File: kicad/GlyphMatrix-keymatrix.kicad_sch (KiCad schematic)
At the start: 153 parts

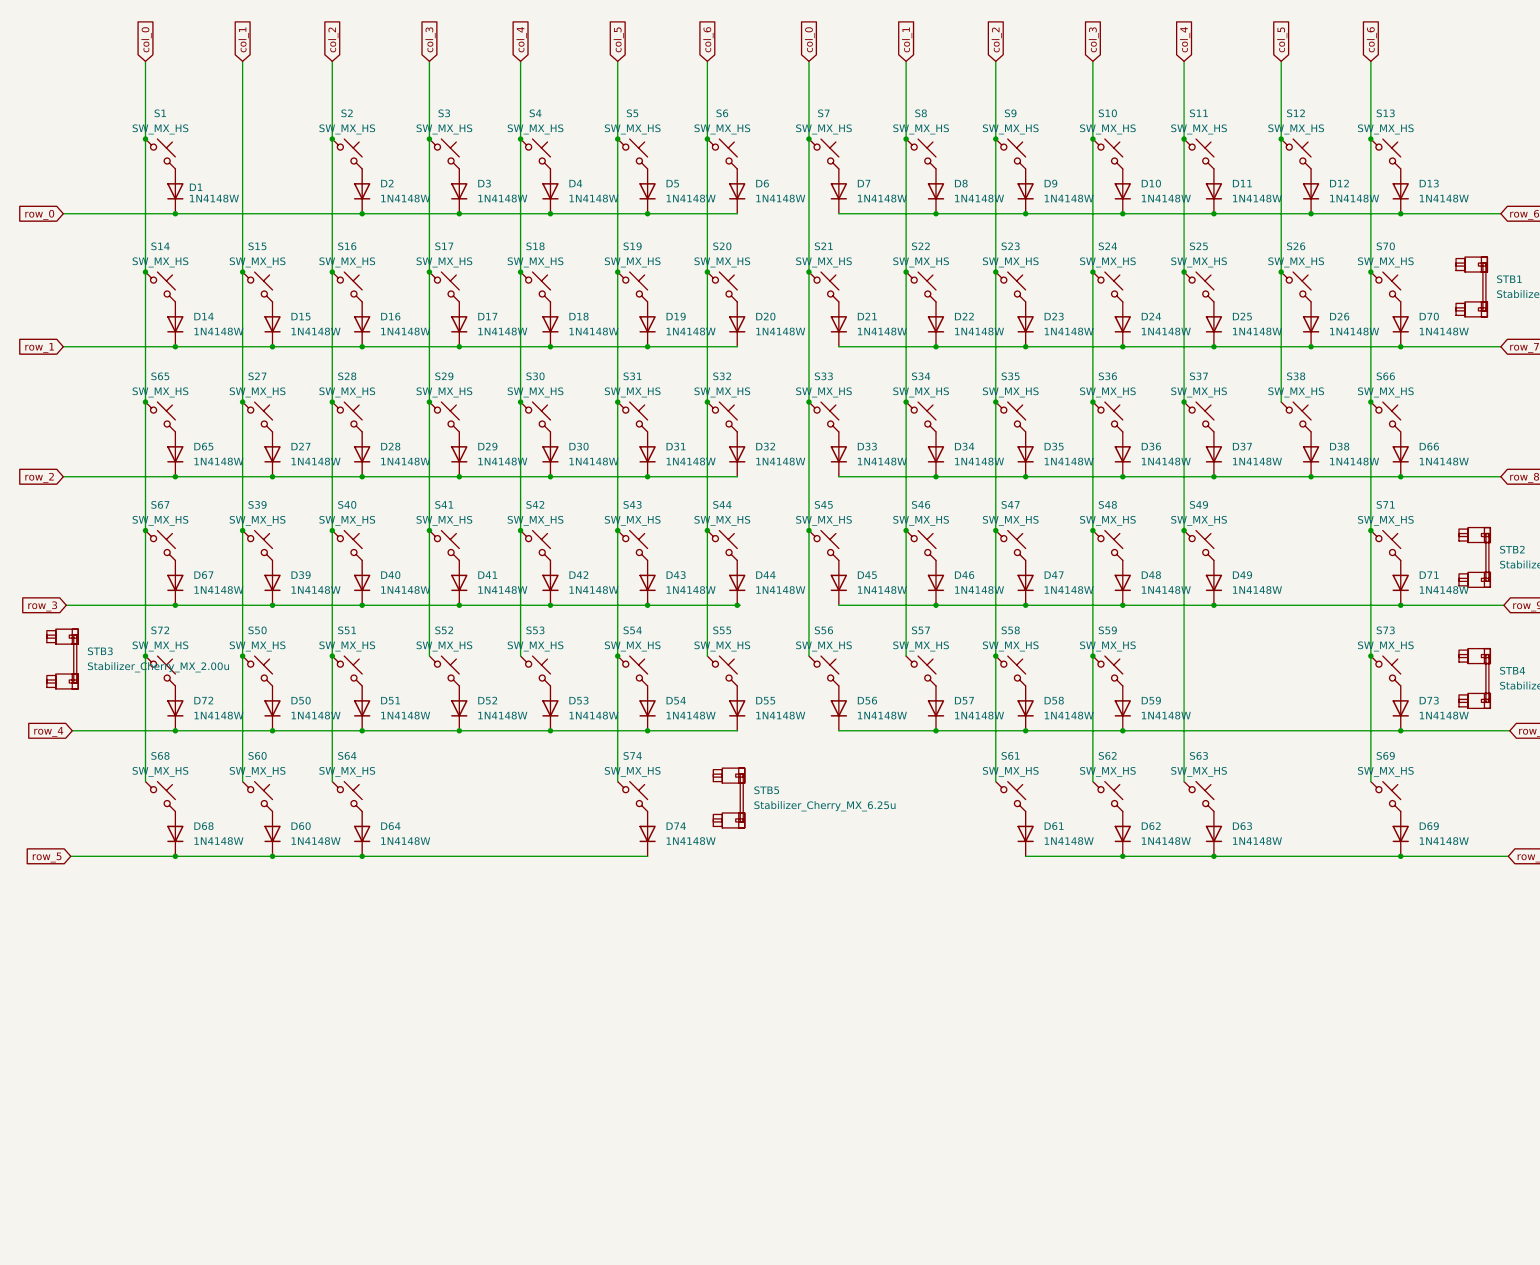
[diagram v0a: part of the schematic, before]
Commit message: added MCU
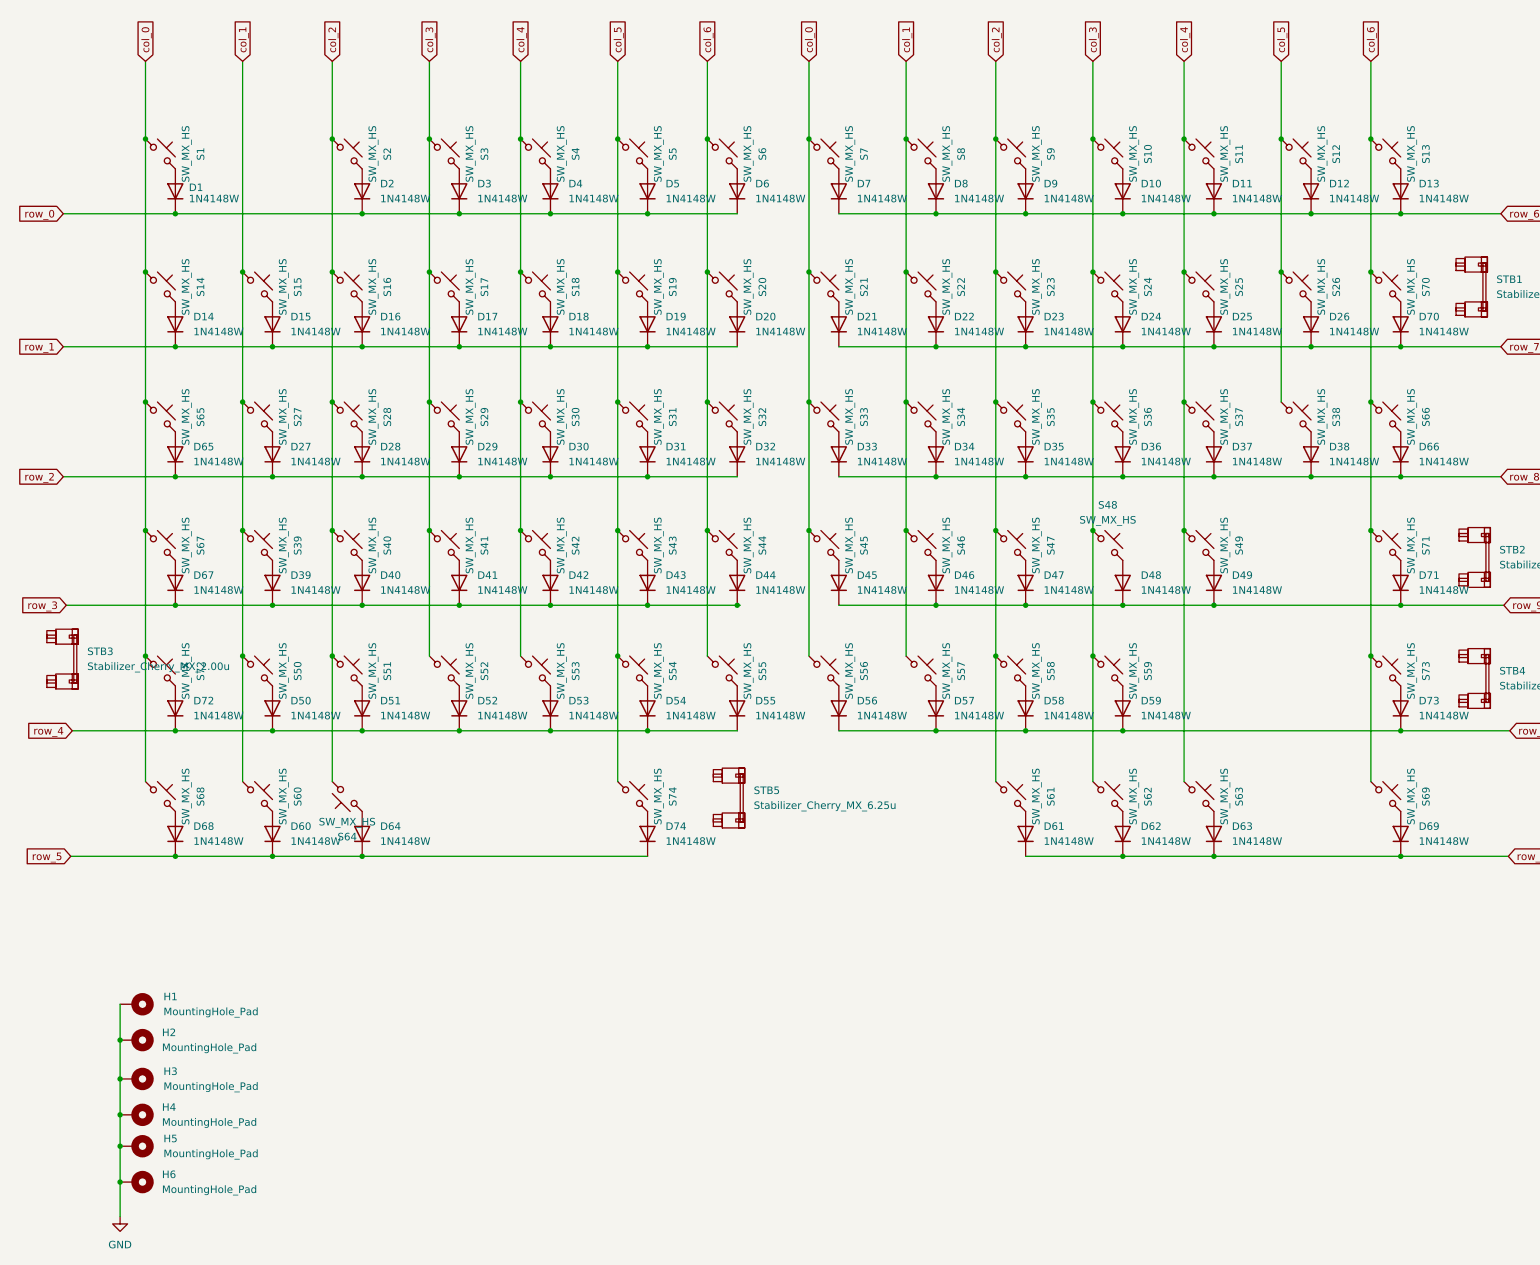
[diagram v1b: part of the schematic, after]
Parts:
- added H1, H2, H3, H4, H5, H6: MountingHole_Pad, TB2086_MISC:MountingHole_3.2mm_Pad, symbol TB2086_MISC:MountingHole_Pad
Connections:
- net col_0: now also S1.2, S14.2, S21.2, S33.2, S45.2, S56.2, S65.2, S67.2, S68.2, S7.2, S72.2; no longer S1.1, S14.1, S21.1, S33.1, S45.1, S56.1, S65.1, S67.1, S68.1, S7.1, S72.1
- net col_1: now also S15.2, S22.2, S27.2, S34.2, S39.2, S46.2, S50.2, S57.2, S60.2, S8.2; no longer S15.1, S22.1, S27.1, S34.1, S39.1, S46.1, S50.1, S57.1, S60.1, S8.1
- net col_2: now also S16.2, S2.2, S23.2, S28.2, S35.2, S40.2, S47.2, S51.2, S58.2, S61.2, S64.2, S9.2; no longer S16.1, S2.1, S23.1, S28.1, S35.1, S40.1, S47.1, S51.1, S58.1, S61.1, S64.1, S9.1
- net col_3: now also S10.2, S17.2, S24.2, S29.2, S3.2, S36.2, S41.2, S52.2, S59.2, S62.2; no longer S10.1, S17.1, S24.1, S29.1, S3.1, S36.1, S41.1, S52.1, S59.1, S62.1
- net col_4: now also S11.2, S18.2, S25.2, S30.2, S37.2, S4.2, S42.2, S49.2, S53.2, S63.2; no longer S11.1, S18.1, S25.1, S30.1, S37.1, S4.1, S42.1, S49.1, S53.1, S63.1
- net col_5: now also S12.2, S19.2, S26.2, S31.2, S38.2, S43.2, S5.2, S54.2, S74.2; no longer S12.1, S19.1, S26.1, S31.1, S38.1, S43.1, S5.1, S54.1, S74.1
- net col_6: now also S13.2, S20.2, S32.2, S44.2, S55.2, S6.2, S66.2, S69.2, S70.2, S71.2, S73.2; no longer S13.1, S20.1, S32.1, S44.1, S55.1, S6.1, S66.1, S69.1, S70.1, S71.1, S73.1
- net at D23.2 (A): now also S23.1; no longer S23.2
- net at D21.2 (A): now also S21.1; no longer S21.2
- net at D34.2 (A): now also S34.1; no longer S34.2
- net at D30.2 (A): now also S30.1; no longer S30.2
- net at D11.2 (A): now also S11.1; no longer S11.2
- net at D27.2 (A): now also S27.1; no longer S27.2
- net at D2.2 (A): now also S2.1; no longer S2.2
- net at D63.2 (A): now also S63.1; no longer S63.2
- net at D71.2 (A): now also S71.1; no longer S71.2
- net at D16.2 (A): now also S16.1; no longer S16.2
- net at D66.2 (A): now also S66.1; no longer S66.2
- net at D41.2 (A): now also S41.1; no longer S41.2
- net at D39.2 (A): now also S39.1; no longer S39.2
- net at D69.2 (A): now also S69.1; no longer S69.2
- net at D19.2 (A): now also S19.1; no longer S19.2
- net at D32.2 (A): now also S32.1; no longer S32.2
- net at D46.2 (A): now also S46.1; no longer S46.2
- net at D53.2 (A): now also S53.1; no longer S53.2
- net at D54.2 (A): now also S54.1; no longer S54.2
- net at D26.2 (A): now also S26.1; no longer S26.2
- net at D59.2 (A): now also S59.1; no longer S59.2
- net at D14.2 (A): now also S14.1; no longer S14.2
- net at D9.2 (A): now also S9.1; no longer S9.2
- net at D15.2 (A): now also S15.1; no longer S15.2
- net at D67.2 (A): now also S67.1; no longer S67.2
- net at D64.2 (A): now also S64.1; no longer S64.2
- net at D73.2 (A): now also S73.1; no longer S73.2
- net at D60.2 (A): now also S60.1; no longer S60.2
- net at D50.2 (A): now also S50.1; no longer S50.2
- net at D44.2 (A): now also S44.1; no longer S44.2
- net at D37.2 (A): now also S37.1; no longer S37.2
- net at D25.2 (A): now also S25.1; no longer S25.2
- net at D72.2 (A): now also S72.1; no longer S72.2
- net at D40.2 (A): now also S40.1; no longer S40.2
- net at D70.2 (A): now also S70.1; no longer S70.2
- net at D20.2 (A): now also S20.1; no longer S20.2
- net at D45.2 (A): now also S45.1; no longer S45.2
- net at D57.2 (A): now also S57.1; no longer S57.2
- net at D74.2 (A): now also S74.1; no longer S74.2
- net at D55.2 (A): now also S55.1; no longer S55.2
- net at D10.2 (A): now also S10.1; no longer S10.2
- net at D43.2 (A): now also S43.1; no longer S43.2
- net at D28.2 (A): now also S28.1; no longer S28.2
- net at D31.2 (A): now also S31.1; no longer S31.2
- net at D29.2 (A): now also S29.1; no longer S29.2
- net at D22.2 (A): now also S22.1; no longer S22.2
- net at D52.2 (A): now also S52.1; no longer S52.2
- net at D68.2 (A): now also S68.1; no longer S68.2
- net at D56.2 (A): now also S56.1; no longer S56.2
- net at D61.2 (A): now also S61.1; no longer S61.2
- net at D4.2 (A): now also S4.1; no longer S4.2
- net at D38.2 (A): now also S38.1; no longer S38.2
- net at D58.2 (A): now also S58.1; no longer S58.2
- net at D13.2 (A): now also S13.1; no longer S13.2
- net at D36.2 (A): now also S36.1; no longer S36.2
- net at D12.2 (A): now also S12.1; no longer S12.2
- net at D49.2 (A): now also S49.1; no longer S49.2
- net at D33.2 (A): now also S33.1; no longer S33.2
- net at D6.2 (A): now also S6.1; no longer S6.2
- net at D51.2 (A): now also S51.1; no longer S51.2
- net at D3.2 (A): now also S3.1; no longer S3.2
- net at D42.2 (A): now also S42.1; no longer S42.2
- net at D7.2 (A): now also S7.1; no longer S7.2
- net at D18.2 (A): now also S18.1; no longer S18.2
- net at D5.2 (A): now also S5.1; no longer S5.2
- net at D35.2 (A): now also S35.1; no longer S35.2
- net at D47.2 (A): now also S47.1; no longer S47.2
- net at D65.2 (A): now also S65.1; no longer S65.2
- net at D24.2 (A): now also S24.1; no longer S24.2
- net at D8.2 (A): now also S8.1; no longer S8.2
- net at D62.2 (A): now also S62.1; no longer S62.2
- net at D17.2 (A): now also S17.1; no longer S17.2
- net at D1.2 (A): now also S1.1; no longer S1.2
- new net GND: H1.1, H2.1, H3.1, H4.1, H5.1, H6.1
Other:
- moved on the sheet: S1, S10, S11, S12, S13, S14, S15, S16, S17, S18, S19, S2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

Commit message: updated MCU
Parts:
- added H7, H8: MountingHole_Pad, TB2086_MISC:MountingHole_3.2mm_Pad, symbol TB2086_MISC:MountingHole_Pad
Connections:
- net GND: now also H7.1, H8.1
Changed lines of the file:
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@@
 	)
 	(junction
+		(at 81.026 254.254)
+		(diameter 0)
+		(color 0 0 0 0)
+	)
+	(junction
 		(at 85.344 159.766)
 		(diameter 0)
@@
 	)
 	(junction
+		(at 81.026 260.35)
+		(diameter 0)
+		(color 0 0 0 0)
+	)
+	(junction
 		(at 106.934 129.286)
 		(diameter 0)
@@
 	(wire
 		(pts
+			(xy 81.026 254.254) (xy 81.026 249.174)
+		)
+		(stroke
+			(width 0)
+			(type default)
+		)
+	)
+	(wire
+		(pts
 			(xy 90.424 172.466) (xy 106.934 172.466)
 		)
@@
 	(wire
 		(pts
+			(xy 81.026 260.35) (xy 81.026 254.254)
+		)
+		(stroke
+			(width 0)
+			(type default)
+		)
+	)
+	(wire
+		(pts
 			(xy 246.38 58.674) (xy 246.38 71.882)
 		)
@@
 	(wire
 		(pts
-			(xy 81.026 255.016) (xy 81.026 249.174)
+			(xy 81.026 262.382) (xy 81.026 260.35)
 		)
 		(stroke
@@
 	)
 	(symbol
+		(lib_id "TB2086_MISC:MountingHole_Pad")
+		(at 83.566 260.35 270)
+		(unit 1)
+		(exclude_from_sim no)
+		(in_bom yes)
+		(on_board yes)
+		(dnp no)
+		(fields_autoplaced yes)
+		(property "Reference" "H8"
+			(at 88.138 259.0799 90)
+			(effects
+				(font
+					(size 1.27 1.27)
+				)
+				(justify left)
+			)
+		)
+		(property "Value" "MountingHole_Pad"
+			(at 88.138 261.6199 90)
+			(effects
+				(font
+					(size 1.27 1.27)
+				)
+				(justify left)
+			)
+		)
+		(property "Footprint" "TB2086_MISC:MountingHole_3.2mm_Pad"
+			(at 83.566 260.35 0)
+			(effects
+				(font
+					(size 1.27 1.27)
+				)
+				(hide yes)
+			)
+		)
+		(property "Datasheet" "~"
+			(at 83.566 260.35 0)
+			(effects
+				(font
+					(size 1.27 1.27)
+				)
+				(hide yes)
+			)
+		)
+		(property "Description" "Mounting Hole with connection"
+			(at 83.566 260.35 0)
+			(effects
+				(font
+					(size 1.27 1.27)
+				)
+				(hide yes)
+			)
+		)
+		(pin "1"
+		)
+		(instances
+			(project "GlyphMatrix"
+				(path "/c7177d09-71a2-4de7-9a3e-bfc16a7f2797/8e27df26-641e-47e6-a7be-c8ba38f472d4"
+					(reference "H8")
+					(unit 1)
+				)
+			)
+		)
+	)
+	(symbol
 		(lib_id "TB2086_KEYSWITCH:SW_MX_HS")
 		(at 104.394 140.97 270)
@@
 	(symbol
 		(lib_id "power:GND")
-		(at 81.026 255.016 0)
+		(at 81.026 262.382 0)
 		(unit 1)
 		(exclude_from_sim no)
@@
 		(fields_autoplaced yes)
 		(property "Reference" "#PWR021"
-			(at 81.026 261.366 0)
+			(at 81.026 268.732 0)
 			(effects
 				(font
@@
 		)
 		(property "Value" "GND"
-			(at 81.026 259.842 0)
+			(at 81.026 267.208 0)
 			(effects
 				(font
@@
 		)
 		(property "Footprint" ""
-			(at 81.026 255.016 0)
+			(at 81.026 262.382 0)
 			(effects
 				(font
@@
 		)
 		(property "Datasheet" ""
-			(at 81.026 255.016 0)
+			(at 81.026 262.382 0)
 			(effects
 				(font
@@
 		)
 		(property "Description" "Power symbol creates a global label with name \"GND\" , ground"
-			(at 81.026 255.016 0)
+			(at 81.026 262.382 0)
 			(effects
 				(font
@@
 					(unit 1)
 				)
+			)
+		)
+	)
+	(symbol
+		(lib_id "TB2086_MISC:MountingHole_Pad")
+		(at 83.566 254.254 270)
+		(unit 1)
+		(exclude_from_sim no)
+		(in_bom yes)
+		(on_board yes)
+		(dnp no)
+		(fields_autoplaced yes)
+		(property "Reference" "H7"
+			(at 88.392 252.9839 90)
+			(effects
+				(font
+					(size 1.27 1.27)
+				)
+				(justify left)
+			)
+		)
+		(property "Value" "MountingHole_Pad"
+			(at 88.392 255.5239 90)
+			(effects
+				(font
+					(size 1.27 1.27)
+				)
+				(justify left)
+			)
+		)
+		(property "Footprint" "TB2086_MISC:MountingHole_3.2mm_Pad"
+			(at 83.566 254.254 0)
+			(effects
+				(font
+					(size 1.27 1.27)
+				)
+				(hide yes)
+			)
+		)
+		(property "Datasheet" "~"
+			(at 83.566 254.254 0)
+			(effects
+				(font
+					(size 1.27 1.27)
+				)
+				(hide yes)
+			)
+		)
+		(property "Description" "Mounting Hole with connection"
+			(at 83.566 254.254 0)
+			(effects
+				(font
+					(size 1.27 1.27)
+				)
+				(hide yes)
+			)
+		)
+		(pin "1"
+		)
+		(instances
+			(project "GlyphMatrix"
+				(path "/c7177d09-71a2-4de7-9a3e-bfc16a7f2797/8e27df26-641e-47e6-a7be-c8ba38f472d4"
+					(reference "H7")
+					(unit 1)
+				)

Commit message: pogo pin connectors
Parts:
- added J2, J5: Conn_01x05, TB2086_MISC:Pogopin_1x05_P2.54mm_Curved, symbol Connector_Generic:Conn_01x05
- added J3, J4, J6, J7: Conn_01x07, TB2086_MISC:Pogopin_1x07_P2.54mm_Curved, symbol Connector_Generic:Conn_01x07
- added LED2: WHITE, LED_SMD:LED_0603_1608Metric_Pad1.05x0.95mm_HandSolder, symbol Device:LED
- added R9: 330, Resistor_SMD:R_0603_1608Metric, symbol Device:R_Small
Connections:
- net GND: now also J2.5 (Pin_5), J5.1 (Pin_1), R9.1
- net col_0 renamed COL0
- net COL0: now also J3.1 (Pin_1), J7.7 (Pin_7)
- net col_1 renamed COL1
- net COL1: now also J3.2 (Pin_2), J7.6 (Pin_6)
- net col_2 renamed COL2
- net COL2: now also J3.3 (Pin_3), J7.5 (Pin_5)
- net col_3 renamed COL3
- net COL3: now also J3.4 (Pin_4), J7.4 (Pin_4)
- net col_4 renamed COL4
- net COL4: now also J3.5 (Pin_5), J7.3 (Pin_3)
- net col_5 renamed COL5
- net COL5: now also J3.6 (Pin_6), J7.2 (Pin_2)
- net col_6 renamed COL6
- net COL6: now also J3.7 (Pin_7), J7.1 (Pin_1)
- net row_0 renamed ROW00
- net row_1 renamed ROW01
- net row_10 renamed ROW10
- net row_11 renamed ROW11
- net row_2 renamed ROW02
- net row_3 renamed ROW03
- net row_4 renamed ROW04
- net row_5 renamed ROW05
- net row_6 renamed ROW06
- net row_7 renamed ROW07
- net row_8 renamed ROW08
- net row_9 renamed ROW09
- new net: LED2.1 (K), R9.2
- new net +5V: J2.1 (Pin_1), J5.5 (Pin_5)
- new net CAPS: LED2.2 (A)
- new net NUM: J2.3 (Pin_3), J5.3 (Pin_3)
- new net RGB_FOM_LEFT: J2.4 (Pin_4)
- new net RGB_FOM_RIGHT: J6.1 (Pin_1)
- new net RGB_TO_LEFT: J4.7 (Pin_7)
- new net RGB_TO_RIGHT: J5.2 (Pin_2)
- new net ROW12: J4.1 (Pin_1), J6.7 (Pin_7)
- new net ROW13: J4.2 (Pin_2), J6.6 (Pin_6)
- new net ROW14: J4.3 (Pin_3), J6.5 (Pin_5)
- new net ROW15: J4.4 (Pin_4), J6.4 (Pin_4)
- new net ROW16: J4.5 (Pin_5), J6.3 (Pin_3)
- new net ROW17: J4.6 (Pin_6), J6.2 (Pin_2)
- new net SCR: J2.2 (Pin_2), J5.4 (Pin_4)

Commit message: screw holes
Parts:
- LED2: value WHITE -> GREEN
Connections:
- net +5V: now also J2.4 (Pin_4), J5.2 (Pin_2); no longer J2.1 (Pin_1), J5.5 (Pin_5)
- net RGB_FOM_LEFT: now also J2.1 (Pin_1); no longer J2.4 (Pin_4)
- net RGB_TO_RIGHT: now also J5.5 (Pin_5); no longer J5.2 (Pin_2)
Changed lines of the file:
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@@
 		)
 	)
-	(global_label "+5V"
+	(global_label "RGB_TO_RIGHT"
 		(shape input)
 		(at 379.73 75.438 0)
@@
 		)
 		(property "Intersheetrefs" "${INTERSHEET_REFS}"
-			(at 386.5857 75.438 0)
+			(at 396.2014 75.438 0)
 			(effects
 				(font
@@
 		)
 	)
-	(global_label "+5V"
+	(global_label "RGB_FOM_LEFT"
 		(shape input)
 		(at 33.782 81.026 180)
@@
 		)
 		(property "Intersheetrefs" "${INTERSHEET_REFS}"
-			(at 26.9263 81.026 0)
+			(at 16.9478 81.026 0)
 			(effects
 				(font
@@
 		)
 	)
-	(global_label "RGB_FOM_LEFT"
+	(global_label "+5V"
 		(shape input)
 		(at 33.782 88.646 180)
@@
 		)
 		(property "Intersheetrefs" "${INTERSHEET_REFS}"
-			(at 16.9478 88.646 0)
+			(at 26.9263 88.646 0)
 			(effects
 				(font
@@
 		)
 	)
-	(global_label "RGB_TO_RIGHT"
+	(global_label "+5V"
 		(shape input)
 		(at 379.73 83.058 0)
@@
 		)
 		(property "Intersheetrefs" "${INTERSHEET_REFS}"
-			(at 396.2014 83.058 0)
+			(at 386.5857 83.058 0)
 			(effects
 				(font
@@
 			)
 		)
-		(property "Value" "WHITE"
+		(property "Value" "GREEN"
 			(at 153.924 227.965 90)
 			(effects

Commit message: artwork
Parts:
- renumbered J2 to POGO1, J5 to POGO2, J3 to POGO3, J7 to POGO4, J4 to POGO5, J6 to POGO6
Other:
- title: (none) -> OmniCode:9001 - GlyphMatrix
- moved on the sheet: POGO2, POGO4, POGO6
